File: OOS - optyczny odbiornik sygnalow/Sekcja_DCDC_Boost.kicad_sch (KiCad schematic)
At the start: 0 parts

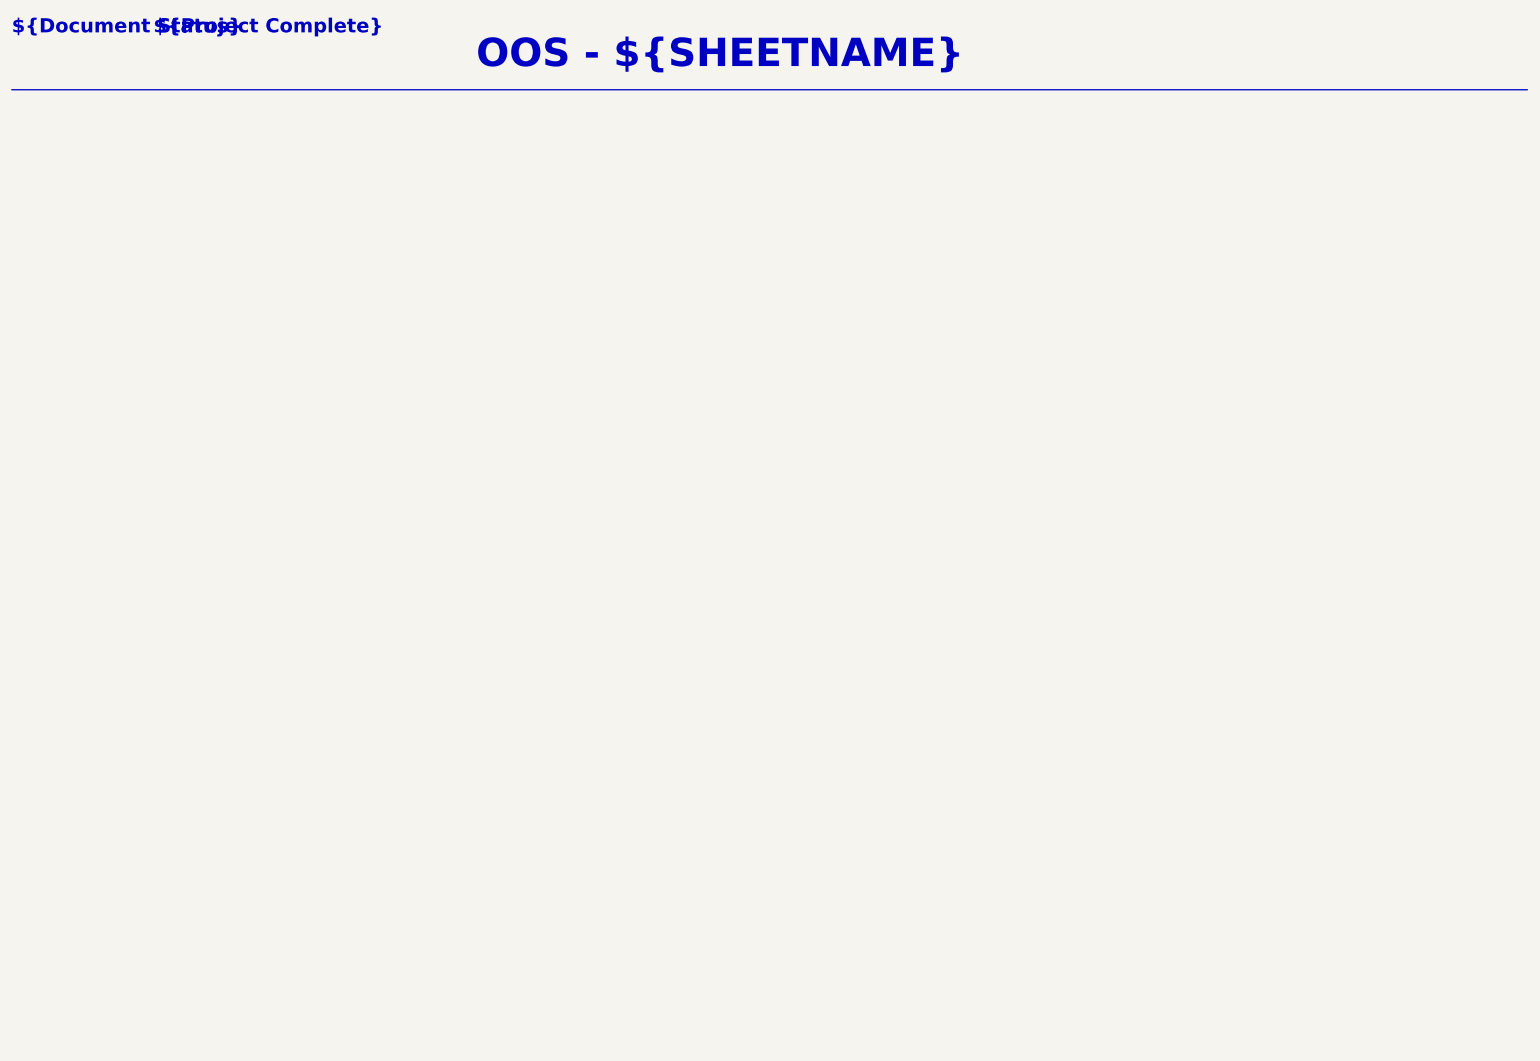
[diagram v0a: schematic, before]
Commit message: Sekcja_DCDC_Boost - gotowa v1.0 schematu. Komponenty maja dodane MPN, linki do datasheetow, zakladek na stronie TME i kluczowe parametry. Dodano opisy Layout notes, Design notes i Project Note w stylu podobnym do Sekcja_Analogowa.kicad_sch. Schemat zawiera takze pola tekstowe z obliczeniami wartosci kluczowych komponentow. Pola tekstowe sa podlaczone do linkow zrodel, z ktorych korzystano do obliczen
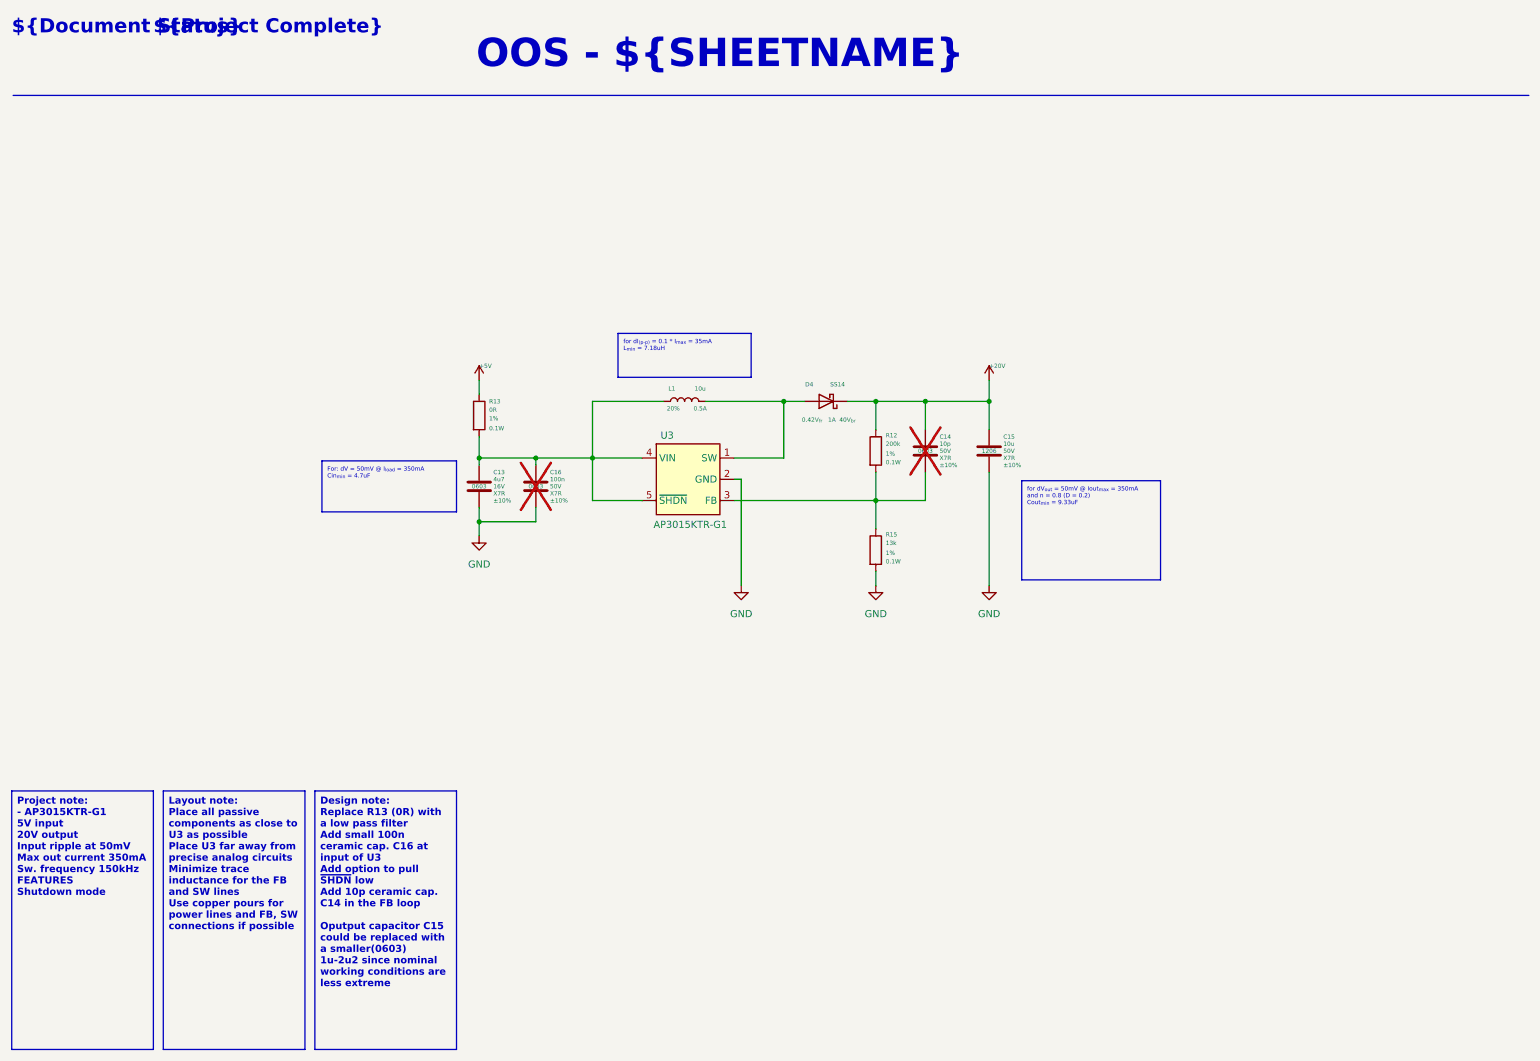
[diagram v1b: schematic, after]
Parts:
- added C13: 4u7, Capacitor_SMD:C_0603_1608Metric, symbol Device:C
- added C14: 10p, Capacitor_SMD:C_0603_1608Metric, symbol Device:C
- added C15: 10u, Capacitor_SMD:C_0603_1608Metric, symbol Device:C
- added C16: 100n, Capacitor_SMD:C_0603_1608Metric, symbol Device:C
- added D4: SS14, Diode_SMD:D_SMA, symbol OOS_Local_Filip:SS14_L_R1
- added L1: 10u, Inductor_SMD:L_0805_2012Metric_Pad1.05x1.20mm_HandSolder, symbol Device:L
- added R12: 200k, Resistor_SMD:R_0603_1608Metric, symbol Device:R
- added R13: 0R, Resistor_SMD:R_0603_1608Metric, symbol Device:R
- added R15: 13k, Resistor_SMD:R_0603_1608Metric, symbol Device:R
- added U3: AP3015KTR-G1, Package_TO_SOT_SMD:SOT-23-5_HandSoldering, symbol OOS_Local_Filip:AP3015KTR-G1
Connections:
- new net: C14.2, R12.2, R15.1, U3.3 (FB)
- new net: D4.2 (A), L1.2, U3.1 (SW)
- new net: C13.1, C16.1, L1.1, R13.2, U3.4 (VIN), U3.5 (~{SHDN})
- new net +20V: C14.1, C15.1, D4.1 (K), R12.1
- new net +5V: R13.1
- new net GND: C13.2, C15.2, C16.2, R15.2, U3.2 (GND)

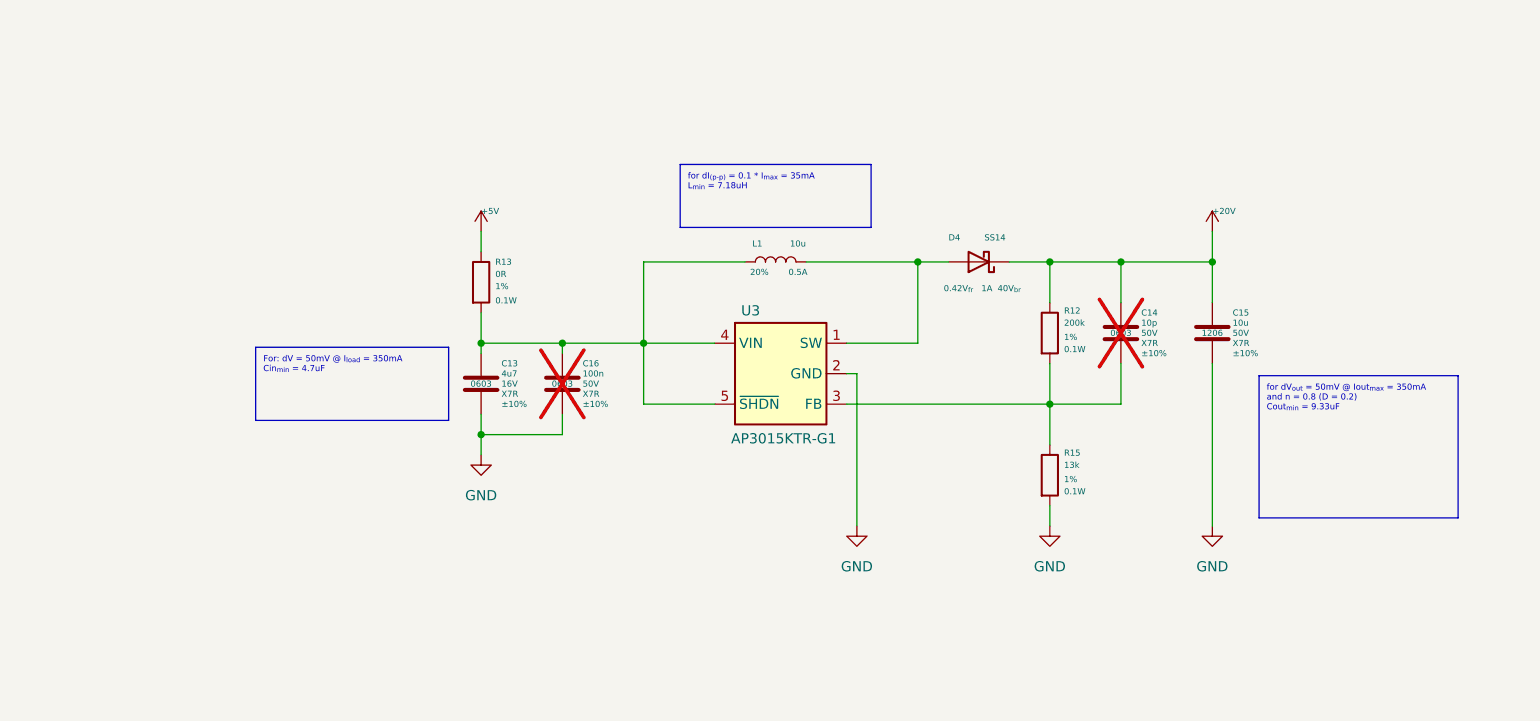
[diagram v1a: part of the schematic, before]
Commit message: Dodane test pointy i net labels. Napiecie wyjsciowe zmienione z 20V na 31.82V (rezystory w FB zmienione). Zmieniona dioda D4 na 60V br, 0.5V forward, 2A. Dodany Jumper na Shutdown pin U3. Dodane 0R na wyjscie przetwornicy (ale moge zmienic na wiecej Watowy). Zmieniony symbol przetwornicy U3 (pin 2 i 3 zamienione miejscami). Zmieniona nazwa GND na 0V
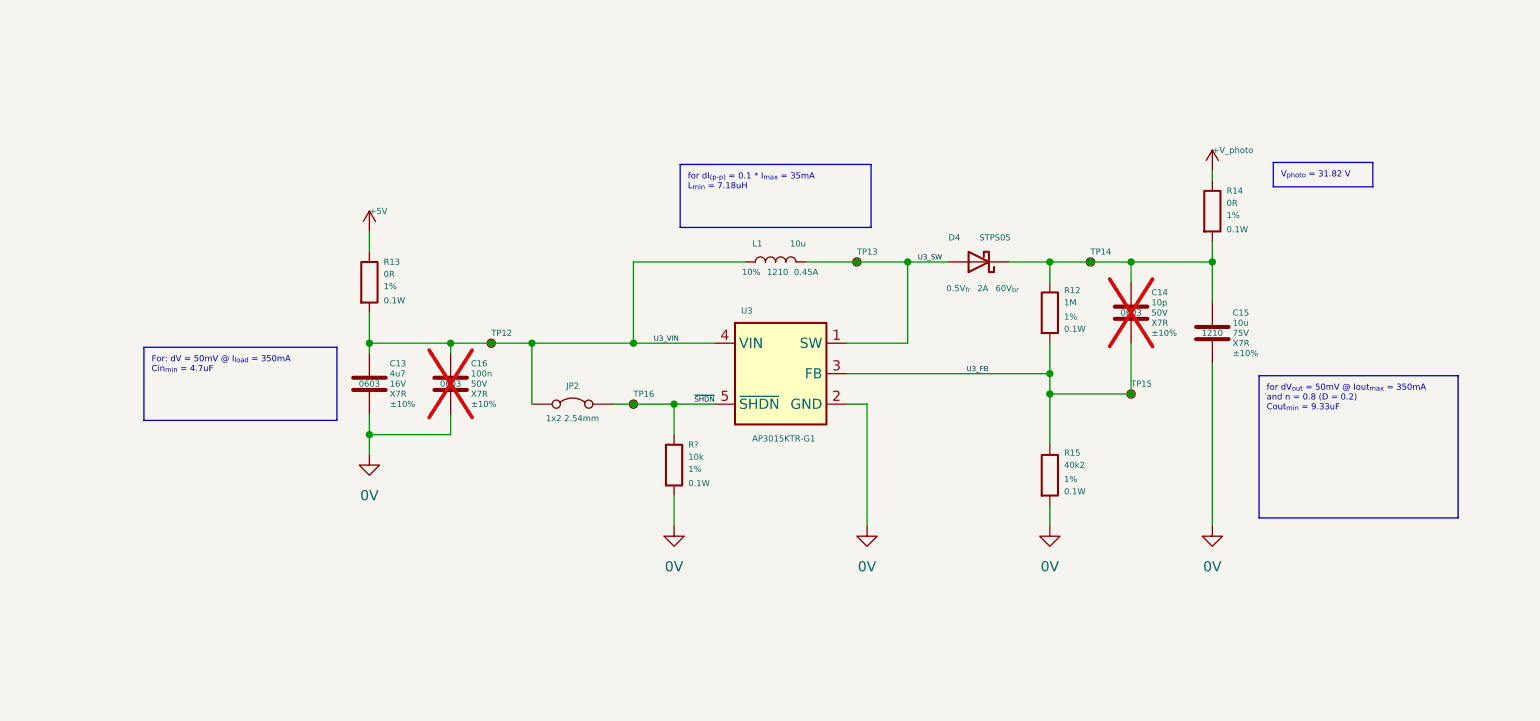
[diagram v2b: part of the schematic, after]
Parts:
- added JP2: 1x2 2.54mm, Connector_PinHeader_2.54mm:PinHeader_1x02_P2.54mm_Vertical, symbol Jumper:Jumper_2_Bridged
- added R14: 0R, Resistor_SMD:R_0603_1608Metric, symbol Device:R
- added R?: 10k, Resistor_SMD:R_0603_1608Metric, symbol Device:R
- added TP12, TP13, TP14, TP15, TP16: TestPoint_Small, TestPoint:TestPoint_Pad_D1.0mm, symbol Connector:TestPoint_Small
- C15: footprint Capacitor_SMD:C_0603_1608Metric -> Capacitor_SMD:C_1210_3225Metric_Pad1.33x2.70mm_HandSolder; MPN  CL31B106KBHNNNE -> CGA6P1X7R1N106K250AC; Package 1206 -> 1210; Supplier Link https://www.tme.eu/pl/en/details/cl31b106kbhnnne/mlcc-smd-c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 -> https://www.tme.eu/pl/en/details/cga6p1x7r1n106kac/mlcc-smd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; Voltage Rating 50V -> 75V
- D4: value SS14 -> STPS05; footprint Diode_SMD:D_SMA -> Diode_SMD:Nexperia_CFP3_SOD-123W; Current 1A -> 2A; Forward V 0.42V_{fr} -> 0.5V_{fr}; MPN SS14L_R1_00001 -> STPS0560Z; Package SMA -> SOD123; Reverse V 40V_{br} -> 60V_{br}; Supplier link https://www.tme.eu/pl/en/details/ss14l-r1/smd-schottky-diod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 -> https://www.tme.eu/pl/en/details/stps0560z/smd-schottky-dio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
- L1: footprint Inductor_SMD:L_0805_2012Metric_Pad1.05x1.20mm_HandSolder -> Inductor_SMD:L_1210_3225Metric_Pad1.42x2.65mm_HandSolder; Current 0.5A -> 0.45A; MPN MLZ2012N100LTD25 -> NLCV32T-100K-EF; Package 0805 -> 1210; Supplier link https://www.tme.eu/pl/en/details/mlz2012n100ltd25/inductors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 -> https://www.tme.eu/pl/en/details/nlcv32t-100k-ef/inductors/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; Tolerance 20% -> 10%
- R12: value 200k -> 1M; MPN WR06X2003FTL -> CRCW06031M00FKEA; Supplier link https://www.tme.eu/pl/details/wr06x2003ftl/rezystory-smd/wa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 -> https://www.tme.eu/pl/en/details/crcw06031m00fkea/smd-resis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
- R15: value 13k -> 40k2; MPN ERJ3EKF1302V -> ERJ3EKF4022V; Supplier link https://www.tme.eu/pl/details/erj3ekf1302v/rezystory-smd/pa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 -> https://www.tme.eu/pl/en/details/erj3ekf4022v/smd-resistors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
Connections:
- net U3_FB: now reaches C14.2, R12.2, R15.1, U3.3 (FB)
- net U3_FB: now also TP15.1
- net U3_SW: now reaches D4.2 (A), L1.2, U3.1 (SW)
- net U3_SW: now also TP13.1
- net U3_VIN: now reaches C13.1, C16.1, L1.1, R13.2, U3.4 (VIN)
- net U3_VIN: now also JP2.1 (A), TP12.1; no longer U3.5 (~{SHDN})
- net +20V: no longer names the net of C14.1, C15.1, D4.1 (K), R12.1
- net +20V: now also R14.2, TP14.1
- net GND renamed 0V
- net 0V: now also R?.2
- new net +V_photo: R14.1
- new net ~{SHDN}: JP2.2 (B), R?.1, TP16.1, U3.5 (~{SHDN})
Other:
- moved on the sheet: C13, C14, C16, R12, R13
